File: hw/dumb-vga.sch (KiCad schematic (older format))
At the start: 22 parts, among them IC1 74HC590N, IC2 74HC590N, IC3 74HC590N, IC4 74HC574N, IC5 74HC574N, IC6 74HC04N, U1 A29040C, X1 VGAF

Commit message: v0.3 Moved inverter
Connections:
- wire segments 168 -> 193
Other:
- moved on the sheet: QG1
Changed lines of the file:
@@
 Title "Dumb VGA"
 Date ""
-Rev "v0.2"
+Rev "v0.3"
 Comp ""
 Comment1 "Simple circuit to generate VGA-like signal"
@@
 L XO-8 QG1
 U 1 1 56DA2917
-P 1500 1400
-F 0 "QG1" H 1200 1725 50  0000 L BNN
-F 1 "XO-8 16MHz" H 1200 1000 50  0000 L BNN
-F 2 "crystal-DIL08S" H 1500 1550 50  0001 C CNN
-F 3 "" H 1500 1400 60  0000 C CNN
-	1    1500 1400
+P 1150 1400
+F 0 "QG1" H 850 1725 50  0000 L BNN
+F 1 "XO-8 16MHz" H 850 1000 50  0000 L BNN
+F 2 "crystal-DIL08S" H 1150 1550 50  0001 C CNN
+F 3 "" H 1150 1400 60  0000 C CNN
+	1    1150 1400
 	1    0    0    -1
 $EndComp
@@
 L VCC #PWR07
 U 1 1 56DA29D7
-P 900 1100
-F 0 "#PWR07" H 900 950 50  0001 C CNN
-F 1 "VCC" H 900 1250 50  0000 C CNN
-F 2 "" H 900 1100 50  0000 C CNN
-F 3 "" H 900 1100 50  0000 C CNN
-	1    900  1100
+P 550 1100
+F 0 "#PWR07" H 550 950 50  0001 C CNN
+F 1 "VCC" H 550 1250 50  0000 C CNN
+F 2 "" H 550 1100 50  0000 C CNN
+F 3 "" H 550 1100 50  0000 C CNN
+	1    550  1100
 	1    0    0    -1
 $EndComp
@@
 L GND #PWR08
 U 1 1 56DA2A09
-P 900 1700
-F 0 "#PWR08" H 900 1450 50  0001 C CNN
-F 1 "GND" H 900 1550 50  0000 C CNN
-F 2 "" H 900 1700 50  0000 C CNN
-F 3 "" H 900 1700 50  0000 C CNN
-	1    900  1700
-	1    0    0    -1
-$EndComp
-NoConn ~ 2000 1200
+P 550 1700
+F 0 "#PWR08" H 550 1450 50  0001 C CNN
+F 1 "GND" H 550 1550 50  0000 C CNN
+F 2 "" H 550 1700 50  0000 C CNN
+F 3 "" H 550 1700 50  0000 C CNN
+	1    550  1700
+	1    0    0    -1
+$EndComp
+NoConn ~ 1650 1200
 $Comp
 L GND #PWR09
@@
 	3350 6650 3350 6750
 Wire Wire Line
-	3350 6750 3700 6750
+	3350 6750 3550 6750
+Wire Wire Line
+	3550 6750 3700 6750
 Wire Wire Line
 	3700 6750 3700 6500
@@
 	3350 6050 3350 5950
 Wire Wire Line
-	3350 5950 3700 5950
+	3350 5950 3550 5950
+Wire Wire Line
+	3550 5950 3700 5950
 Wire Wire Line
 	3700 5950 3700 6200
 Connection ~ 3550 5950
 Wire Wire Line
-	2650 5950 3000 5950
+	2650 5950 2850 5950
+Wire Wire Line
+	2850 5950 3000 5950
 Wire Wire Line
 	3000 5950 3000 6200
@@
 	2650 6650 2650 6750
 Wire Wire Line
-	2650 6750 3000 6750
+	2650 6750 2850 6750
+Wire Wire Line
+	2850 6750 3000 6750
 Wire Wire Line
 	3000 6750 3000 6500
 Connection ~ 2850 6750
 Wire Wire Line
-	1950 6750 2300 6750
+	1950 6750 2150 6750
+Wire Wire Line
+	2150 6750 2300 6750
 Wire Wire Line
 	2300 6750 2300 6500
@@
 	2300 5950 2300 6200
 Wire Wire Line
-	1950 5950 2300 5950
+	1950 5950 2150 5950
+Wire Wire Line
+	2150 5950 2300 5950
 Wire Wire Line
 	1950 5950 1950 6050
@@
 	5050 3200 5050 4900
 Wire Wire Line
-	900  1100 900  1200
-Wire Wire Line
-	900  1200 1000 1200
-Wire Wire Line
-	900  1700 900  1600
-Wire Wire Line
-	900  1600 1000 1600
+	550  1100 550  1200
+Wire Wire Line
+	550  1200 650  1200
+Wire Wire Line
+	550  1700 550  1600
+Wire Wire Line
+	550  1600 650  1600
 Connection ~ 2700 1400
 Wire Wire Line
@@
 	2850 4200 2900 4200
 Wire Wire Line
-	2700 1400 2700 4600
+	2700 1400 2700 1800
+Wire Wire Line
+	2700 1800 2700 2800
+Wire Wire Line
+	2700 2800 2700 3200
+Wire Wire Line
+	2700 3200 2700 4600
 Wire Wire Line
 	2900 1800 2700 1800
@@
 	1200 6500 1200 6750
 Wire Wire Line
-	1200 6750 1600 6750
+	1200 6750 1400 6750
+Wire Wire Line
+	1400 6750 1600 6750
 Wire Wire Line
 	1600 6750 1600 6500
@@
 	1600 5950 1600 6200
 Wire Wire Line
-	1200 5950 1600 5950
+	1200 5950 1400 5950
+Wire Wire Line
+	1400 5950 1600 5950
 Wire Wire Line
 	1200 5950 1200 6200
@@
 	9250 2250 9300 2250
 Wire Wire Line
-	9250 1350 9250 2350
+	9250 1350 9250 1550
+Wire Wire Line
+	9250 1550 9250 1750
+Wire Wire Line
+	9250 1750 9250 2150
+Wire Wire Line
+	9250 2150 9250 2250
+Wire Wire Line
+	9250 2250 9250 2350
 Wire Wire Line
 	9400 2150 9250 2150
@@
 	9150 1350 9150 1450
 Wire Wire Line
-	9100 1450 9300 1450
+	9100 1450 9150 1450
+Wire Wire Line
+	9150 1450 9300 1450
 Connection ~ 9150 1450
 Wire Wire Line
 	8850 1600 9150 1600
 Wire Wire Line
-	9150 1600 9150 1700
+	9150 1600 9150 1650
+Wire Wire Line
+	9150 1650 9150 1700
 Wire Wire Line
 	9150 1700 9100 1700
@@
 Connection ~ 9150 1650
 Wire Wire Line
-	8850 1850 9300 1850
+	8850 1850 9150 1850
+Wire Wire Line
+	9150 1850 9300 1850
 Wire Wire Line
 	9150 1850 9150 1950
@@
 	5300 3500 5200 3500
 Wire Wire Line
-	5200 3500 5200 3700
+	5200 3500 5200 3600
+Wire Wire Line
+	5200 3600 5200 3700
 Wire Wire Line
 	5300 3600 5200 3600
 Connection ~ 5200 3600
 Wire Wire Line
-	2000 1400 2900 1400
+	2500 1400 2600 1400
+Wire Wire Line
+	2600 1400 2700 1400
+Wire Wire Line
+	2700 1400 2900 1400
 $Comp
 L 74HC574N IC4
@@
 	6900 2300 7000 2300
 Wire Wire Line
-	2500 900  2500 1400
-Connection ~ 2500 1400
+	2600 1150 2600 1400
+Connection ~ 2600 1400
 $Comp
 L 74HC574N IC5
@@
 	4400 6750 4400 6500
 Wire Wire Line
-	4050 6750 4400 6750
+	4050 6750 4250 6750
+Wire Wire Line
+	4250 6750 4400 6750
 Wire Wire Line
 	4050 6750 4050 6650
@@
 	4050 6050 4050 5950
 Wire Wire Line
-	4050 5950 4400 5950
+	4050 5950 4250 5950
+Wire Wire Line
+	4250 5950 4400 5950
 Wire Wire Line
 	4400 5950 4400 6200
@@
 L 74HC04N IC6
 U 1 1 56DBE569
-P 6000 900
-F 0 "IC6" H 6100 1025 50  0000 L BNN
-F 1 "74HC04N" H 6100 700 50  0000 L BNN
-F 2 "74xx-eu-DIL14" H 6000 1050 50  0001 C CNN
-F 3 "" H 6000 900 60  0000 C CNN
-	1    6000 900
-	1    0    0    -1
-$EndComp
-Wire Wire Line
-	6400 900  6900 900
-Wire Wire Line
-	6900 900  6900 2300
-Wire Wire Line
-	5600 900  2500 900
+P 2100 1400
+F 0 "IC6" H 2200 1525 50  0000 L BNN
+F 1 "74HC04N" H 2200 1200 50  0000 L BNN
+F 2 "74xx-eu-DIL14" H 2100 1550 50  0001 C CNN
+F 3 "" H 2100 1400 60  0000 C CNN
+	1    2100 1400
+	1    0    0    -1
+$EndComp
+Wire Wire Line
+	2600 1150 6900 1150
+Wire Wire Line
+	6900 1150 6900 2300
 $Comp
 L 74HC04N IC6
@@
 	4750 6650 4750 6750
 Wire Wire Line
-	4750 6750 5100 6750
+	4750 6750 4950 6750
+Wire Wire Line
+	4950 6750 5100 6750
 Wire Wire Line
 	5100 6750 5100 6500
@@
 	5100 5950 5100 6200
 Wire Wire Line
-	4750 5950 5100 5950
+	4750 5950 4950 5950
+Wire Wire Line
+	4950 5950 5100 5950
 Wire Wire Line
 	4750 6050 4750 5950
@@
 	5050 4900 3900 4900
 NoConn ~ 3900 4400
+Wire Wire Line
+	1650 1400 1700 1400
 $EndSCHEMATC

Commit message: Eliminated inverter
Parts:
- removed C7: 0.1u, symbol C
- removed IC6: 74HC04N, 74xx-eu-DIL14, symbol 74HC04N
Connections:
- wire segments 193 -> 164
- no-connect marks 14 -> 13
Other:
- moved on the sheet: IC4A, QG1, R1, R2, R3, R4, R5, R6, U1, X1

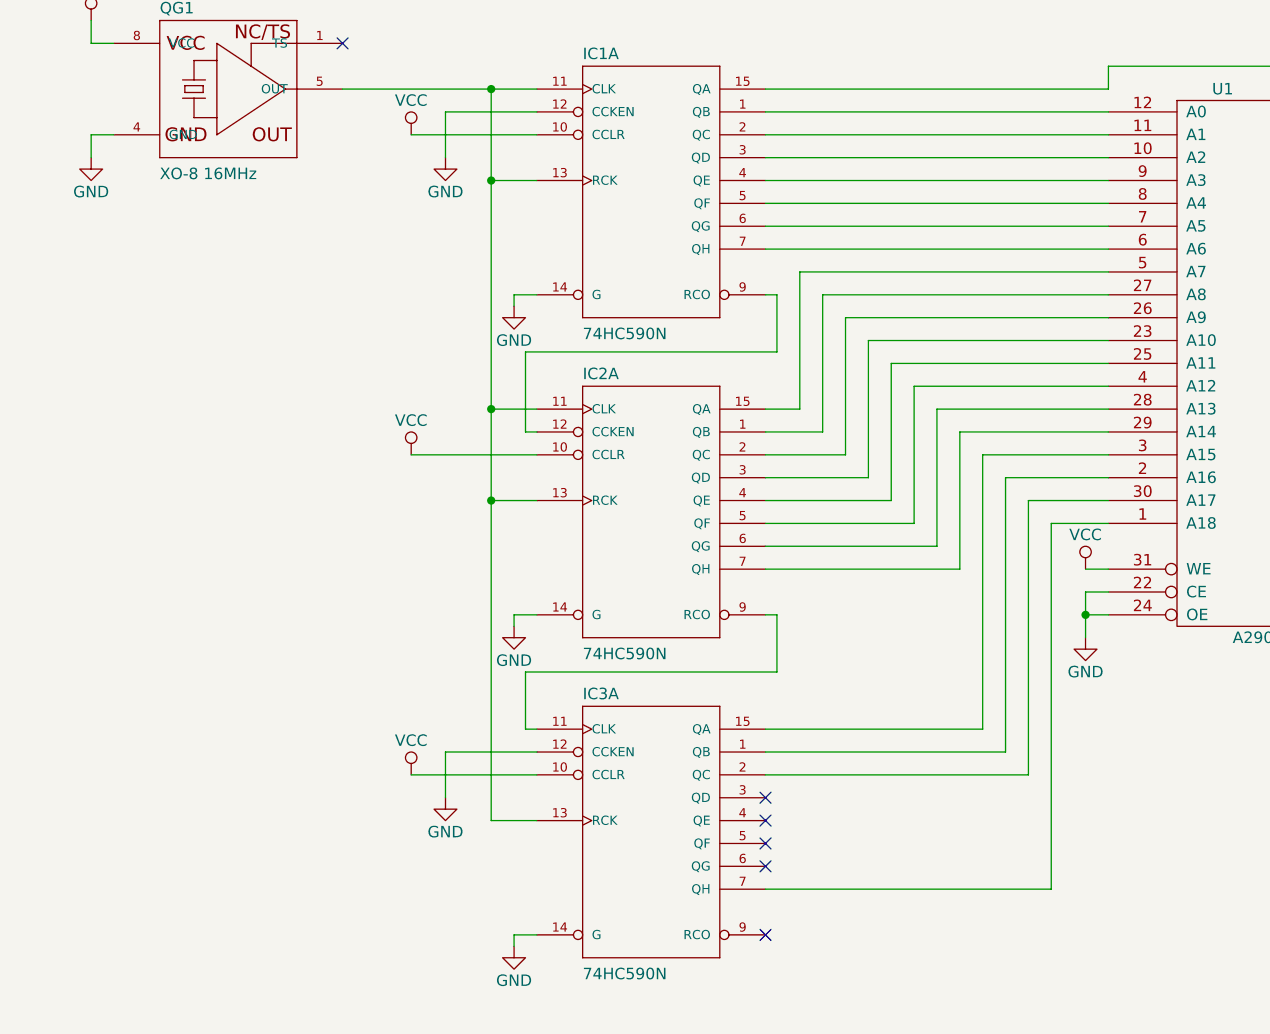
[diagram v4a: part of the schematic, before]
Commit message: FIXME: Scan-line doubling
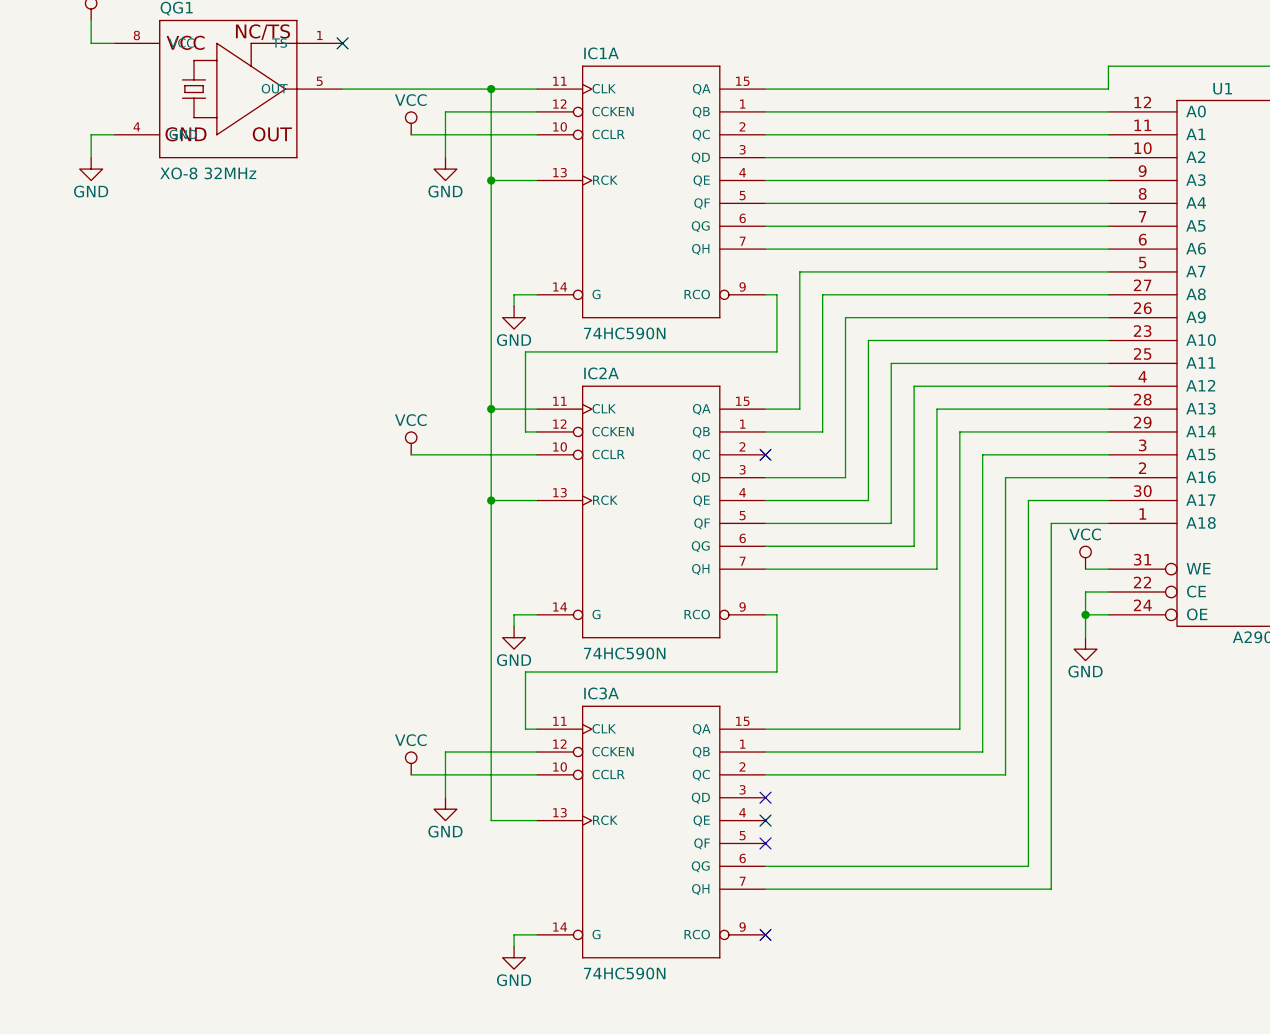
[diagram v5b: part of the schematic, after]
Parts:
- QG1: value XO-8 16MHz -> XO-8 32MHz
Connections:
- net at IC2.2 (QC): no longer U1.26 (A9)
- net at IC2.3 (QD): now also U1.26 (A9); no longer U1.23 (A10)
- net at IC2.4 (QE): now also U1.23 (A10); no longer U1.25 (A11)
- net at IC2.5 (QF): now also U1.25 (A11); no longer U1.4 (A12)
- net at IC2.6 (QG): now also U1.4 (A12); no longer U1.28 (A13)
- net at IC2.7 (QH): now also U1.28 (A13); no longer U1.29 (A14)
- net at IC3.1 (QB): now also U1.3 (A15); no longer U1.2 (A16)
- net at IC3.15 (QA): now also U1.29 (A14); no longer U1.3 (A15)
- net at IC3.2 (QC): now also U1.2 (A16); no longer U1.30 (A17)
- net at IC3.6 (QG): now also U1.30 (A17)
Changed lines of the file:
@@
 Title "Dumb VGA"
 Date ""
-Rev "v0.3"
+Rev "v0.4"
 Comp ""
 Comment1 "Simple circuit to generate VGA-like signal"
@@
 $EndComp
 $Comp
-L 74HC590N IC2
-U 1 1 56DA18AE
-P 3400 3200
-F 0 "IC2" H 3100 3725 50  0000 L BNN
-F 1 "74HC590N" H 3100 2500 50  0000 L BNN
-F 2 "74xx-eu-DIL16" H 3400 3350 50  0001 C CNN
-F 3 "" H 3400 3200 60  0000 C CNN
-	1    3400 3200
-	1    0    0    -1
-$EndComp
-$Comp
 L 74HC590N IC3
 U 1 1 56DA1926
@@
 NoConn ~ 3900 4600
 NoConn ~ 3900 4700
-NoConn ~ 3900 4800
 $Comp
 L XO-8 QG1
@@
 P 1550 1400
 F 0 "QG1" H 1250 1725 50  0000 L BNN
-F 1 "XO-8 16MHz" H 1250 1000 50  0000 L BNN
+F 1 "XO-8 32MHz" H 1250 1000 50  0000 L BNN
 F 2 "crystal-DIL08S" H 1550 1550 50  0001 C CNN
 F 3 "" H 1550 1400 60  0000 C CNN
@@
 	4150 2300 5400 2300
 Wire Wire Line
-	3900 3000 4250 3000
-Wire Wire Line
-	4250 3000 4250 2400
-Wire Wire Line
-	4250 2400 5400 2400
-Wire Wire Line
-	3900 3100 4350 3100
-Wire Wire Line
-	4350 3100 4350 2500
+	4350 2500 4350 3200
 Wire Wire Line
 	4350 2500 5400 2500
 Wire Wire Line
-	3900 3200 4450 3200
-Wire Wire Line
-	4450 3200 4450 2600
+	4450 2600 4450 3300
 Wire Wire Line
 	4450 2600 5400 2600
 Wire Wire Line
-	3900 3300 4550 3300
-Wire Wire Line
-	4550 3300 4550 2700
+	4550 2700 4550 3400
 Wire Wire Line
 	4550 2700 5400 2700
 Wire Wire Line
-	3900 3400 4650 3400
-Wire Wire Line
-	4650 3400 4650 2800
+	4650 2800 4650 3500
 Wire Wire Line
 	4650 2800 5400 2800
 Wire Wire Line
-	3900 3500 4750 3500
-Wire Wire Line
-	4750 3500 4750 2900
+	4750 2900 4750 4200
 Wire Wire Line
 	4750 2900 5400 2900
@@
 	5400 3000 4850 3000
 Wire Wire Line
-	4850 3000 4850 4200
-Wire Wire Line
-	4850 4200 3900 4200
+	4850 3000 4850 4300
 Wire Wire Line
 	5400 3100 4950 3100
 Wire Wire Line
-	4950 3100 4950 4300
-Wire Wire Line
-	4950 4300 3900 4300
+	4950 3100 4950 4400
 Wire Wire Line
 	950  1100 950  1200
@@
 	5400 3700 5300 3700
 Wire Wire Line
-	3900 4400 5050 4400
-Wire Wire Line
-	5050 4400 5050 3200
+	5050 3200 5050 4800
 Wire Wire Line
 	5050 3200 5400 3200
@@
 Wire Wire Line
 	5400 1300 5400 1400
+Wire Wire Line
+	5400 2400 4250 2400
+$Comp
+L 74HC590N IC2
+U 1 1 56DA18AE
+P 3400 3200
+F 0 "IC2" H 3100 3725 50  0000 L BNN
+F 1 "74HC590N" H 3100 2500 50  0000 L BNN
+F 2 "74xx-eu-DIL16" H 3400 3350 50  0001 C CNN
+F 3 "" H 3400 3200 60  0000 C CNN
+	1    3400 3200
+	1    0    0    -1
+$EndComp
+NoConn ~ 3900 3000
+Wire Wire Line
+	3900 3100 4250 3100
+Wire Wire Line
+	4250 3100 4250 2400
+Wire Wire Line
+	4350 3200 3900 3200
+Wire Wire Line
+	4450 3300 3900 3300
+Wire Wire Line
+	4550 3400 3900 3400
+Wire Wire Line
+	4650 3500 3900 3500
+Wire Wire Line
+	4750 4200 3900 4200
+Wire Wire Line
+	4850 4300 3900 4300
+Wire Wire Line
+	4950 4400 3900 4400
+Wire Wire Line
+	5050 4800 3900 4800
 $EndSCHEMATC
